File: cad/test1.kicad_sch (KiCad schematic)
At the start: 2 parts

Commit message: docs added
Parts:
- added BT?: Battery, symbol Device:Battery
- added M? (x2): Motor_DC, symbol Motor:Motor_DC
- added U?: MemsicIMU380, symbol teetest:MemsicIMU380
- gave numbers to parts that had none: 1
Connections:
- net at M.~ (VREG): now also BT?.2 (-)
- new net: M.~ (VREG), M?.1 (+) (x2)
- new net: M.~ (VREG), M?.2 (-) (x2)
- new net: BT?.1 (+), M.~ (VREG)
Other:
- moved on the sheet: M, U?

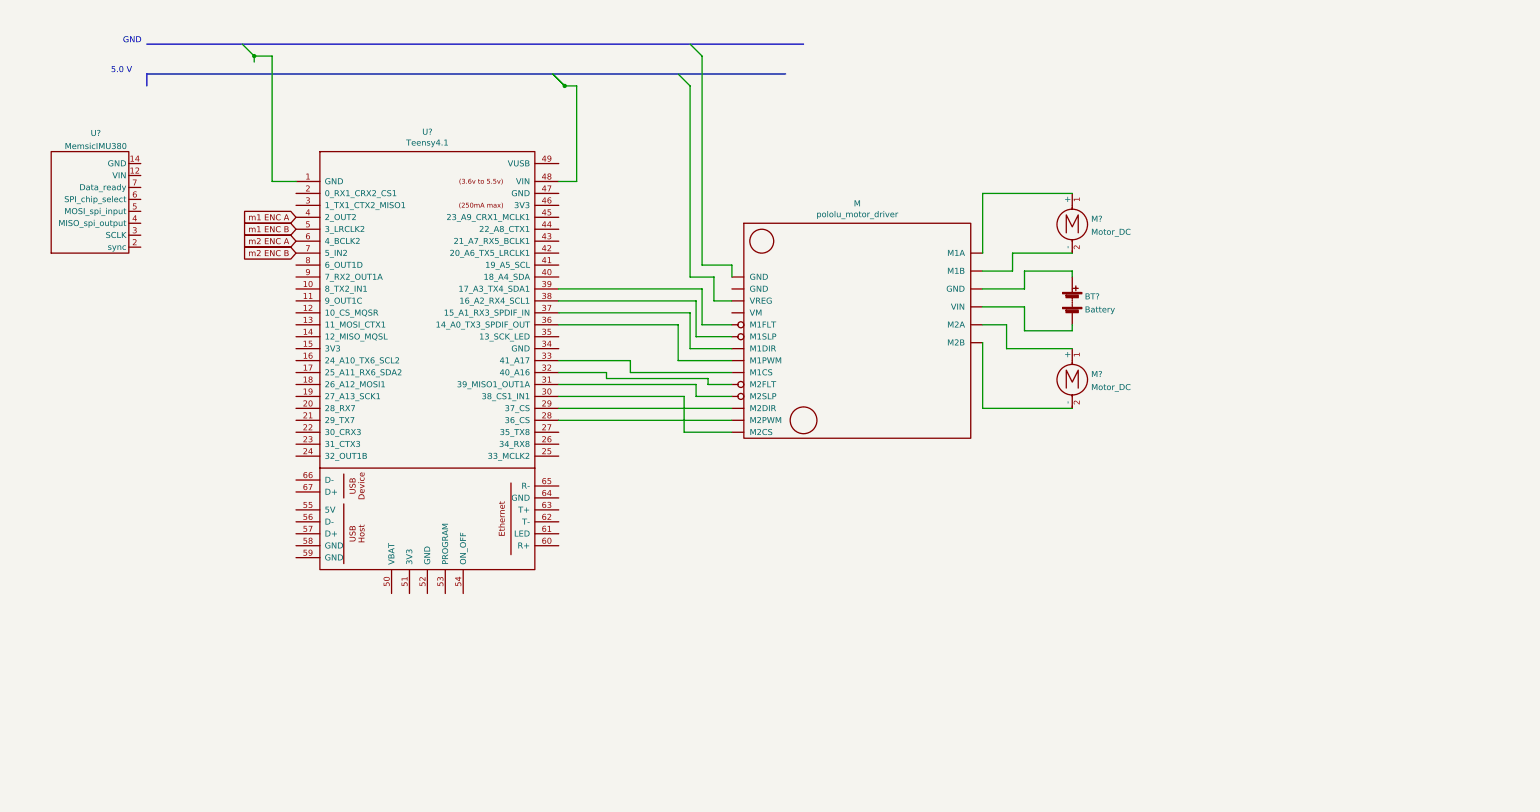
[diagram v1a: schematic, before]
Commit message: audio lib added
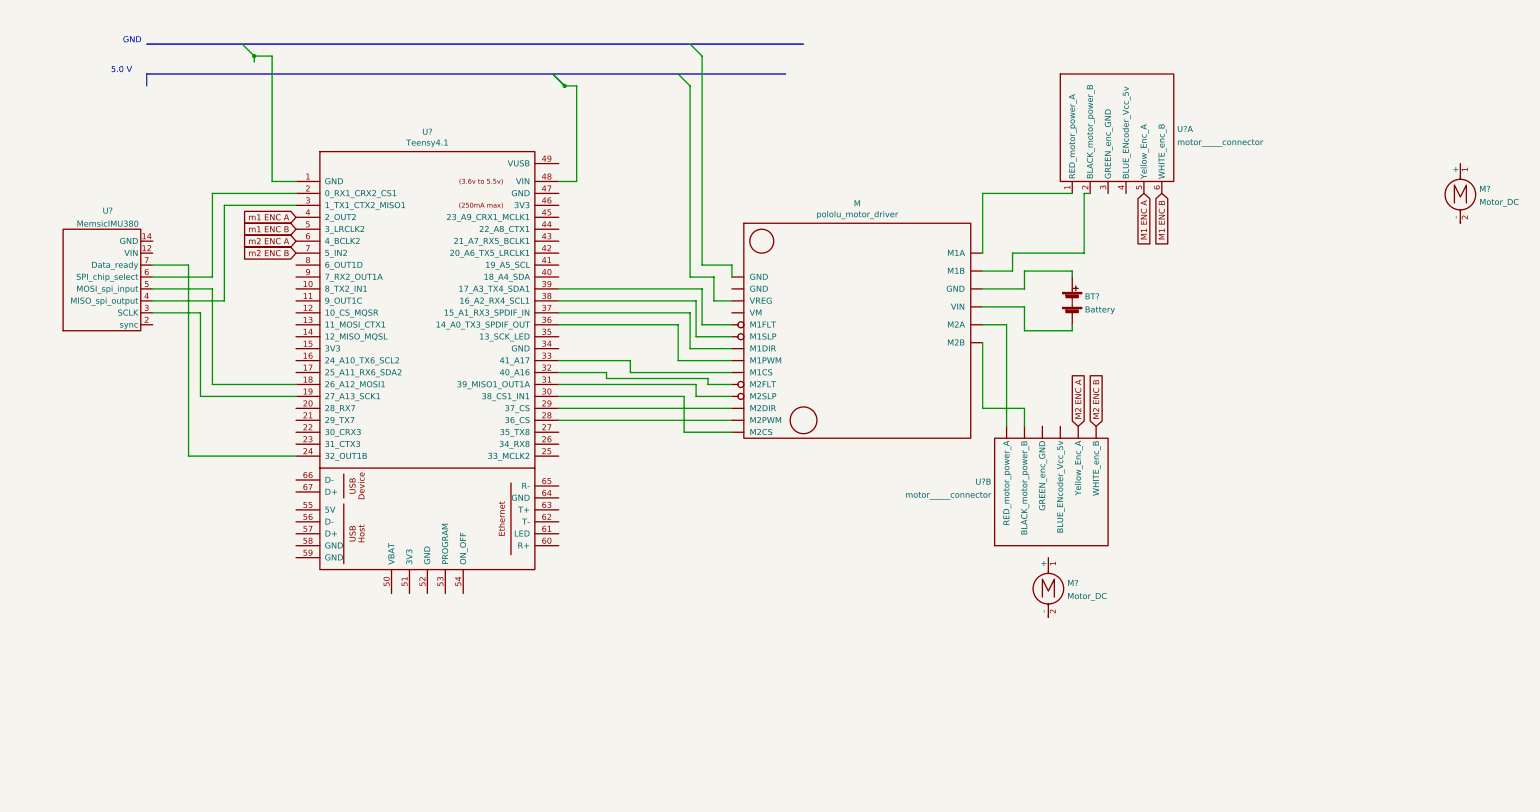
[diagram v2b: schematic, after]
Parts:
- added U? (x2): motor_____connector, symbol teetest:motor_____connector
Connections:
- net at U?.18 (26_A12_MOSI1): now also U?.5 (MOSI_spi_input)
- net at U?.19 (27_A13_SCK1): now also U?.3 (SCLK)
- net at U?.2 (0_RX1_CRX2_CS1): now also U?.6 (SPI_chip_select)
- net at U?.24 (32_OUT1B): now also U?.7 (Data_ready)
- net at U?.3 (1_TX1_CTX2_MISO1): now also U?.4 (MISO_spi_output)
- net at M.~ (VREG): now also BT?.2 (-)
- net at M?.1 (+): no longer M.~ (VREG) (x2)
- net at M?.2 (-): no longer M.~ (VREG) (x2)
- new net: M.~ (VREG), U?.-UB (Yellow_Enc_A)
- new net: M.~ (VREG), U?.1-UB (RED_motor_power_A)
- new net: M.~ (VREG), U?.1 (RED_motor_power_A)
- new net: M.~ (VREG), U?.2 (BLACK_motor_power_B)
- new net M1 ENC A: U?.5 (Yellow_Enc_A)
- new net M1 ENC B: U?.6 (WHITE_enc_B)
- new net M2 ENC A: U?.-UB (Yellow_Enc_A)
- new net M2 ENC B: U?.6-UB (WHITE_enc_B)
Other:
- moved on the sheet: M?, U?
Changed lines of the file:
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@@
+    (stroke (width 0) (type default) (color 0 0 0 0))
+  )
+  (wire (pts (xy 49.53 74.93) (xy 57.15 74.93))
+    (stroke (width 0) (type default) (color 0 0 0 0))
+  )
+  (wire (pts (xy 49.53 77.47) (xy 62.23 77.47))
+    (stroke (width 0) (type default) (color 0 0 0 0))
+  )
+  (wire (pts (xy 49.53 80.01) (xy 62.23 80.01))
+    (stroke (width 0) (type default) (color 0 0 0 0))
+  )
+  (wire (pts (xy 49.53 82.55) (xy 64.77 82.55))
+    (stroke (width 0) (type default) (color 0 0 0 0))
+  )
+  (wire (pts (xy 49.53 85.09) (xy 59.69 85.09))
+    (stroke (width 0) (type default) (color 0 0 0 0))
+  )
+  (wire (pts (xy 57.15 74.93) (xy 57.15 115.57))
+    (stroke (width 0) (type default) (color 0 0 0 0))
+  )
+  (wire (pts (xy 57.15 115.57) (xy 80.01 115.57))
+    (stroke (width 0) (type default) (color 0 0 0 0))
+  )
+  (wire (pts (xy 59.69 85.09) (xy 59.69 102.87))
+    (stroke (width 0) (type default) (color 0 0 0 0))
+  )
+  (wire (pts (xy 59.69 102.87) (xy 80.01 102.87))
+    (stroke (width 0) (type default) (color 0 0 0 0))
+  )
+  (wire (pts (xy 62.23 59.69) (xy 80.01 59.69))
+    (stroke (width 0) (type default) (color 0 0 0 0))
+  )
+  (wire (pts (xy 62.23 77.47) (xy 62.23 59.69))
+    (stroke (width 0) (type default) (color 0 0 0 0))
+  )
+  (wire (pts (xy 62.23 80.01) (xy 62.23 100.33))
+    (stroke (width 0) (type default) (color 0 0 0 0))
+  )
+  (wire (pts (xy 62.23 100.33) (xy 80.01 100.33))
+    (stroke (width 0) (type default) (color 0 0 0 0))
+  )
+  (wire (pts (xy 64.77 62.23) (xy 80.01 62.23))
+    (stroke (width 0) (type default) (color 0 0 0 0))
+  )
+  (wire (pts (xy 64.77 82.55) (xy 64.77 62.23))
     (stroke (width 0) (type default) (color 0 0 0 0))
   )
@@
     (stroke (width 0) (type default) (color 0 0 0 0))
   )
-  (wire (pts (xy 226.06 105.41) (xy 245.11 105.41))
-    (stroke (width 0) (type default) (color 0 0 0 0))
-  )
-  (wire (pts (xy 231.14 87.63) (xy 231.14 92.71))
-    (stroke (width 0) (type default) (color 0 0 0 0))
-  )
-  (wire (pts (xy 231.14 92.71) (xy 245.11 92.71))
-    (stroke (width 0) (type default) (color 0 0 0 0))
-  )
-  (wire (pts (xy 232.41 72.39) (xy 245.11 72.39))
+  (wire (pts (xy 226.06 105.41) (xy 234.95 105.41))
+    (stroke (width 0) (type default) (color 0 0 0 0))
+  )
+  (wire (pts (xy 231.14 87.63) (xy 231.14 109.22))
+    (stroke (width 0) (type default) (color 0 0 0 0))
+  )
+  (wire (pts (xy 232.41 72.39) (xy 247.65 72.39))
     (stroke (width 0) (type default) (color 0 0 0 0))
   )
@@
     (stroke (width 0) (type default) (color 0 0 0 0))
   )
+  (wire (pts (xy 234.95 105.41) (xy 234.95 109.22))
+    (stroke (width 0) (type default) (color 0 0 0 0))
+  )
   (wire (pts (xy 245.11 76.2) (xy 245.11 77.47))
     (stroke (width 0) (type default) (color 0 0 0 0))
   )
   (wire (pts (xy 245.11 87.63) (xy 245.11 88.9))
+    (stroke (width 0) (type default) (color 0 0 0 0))
+  )
+  (wire (pts (xy 247.65 59.69) (xy 247.65 72.39))
+    (stroke (width 0) (type default) (color 0 0 0 0))
+  )
+  (wire (pts (xy 248.92 59.69) (xy 247.65 59.69))
     (stroke (width 0) (type default) (color 0 0 0 0))
   )
@@
     )
   )
+  (global_label "M2 ENC A" (shape input) (at 246.38 109.22 90) (fields_autoplaced)
+    (effects (font (size 1.27 1.27)) (justify left))
+    (property "Intersheet References" "${INTERSHEET_REFS}" (id 0) (at 246.3006 97.3726 90)
+      (effects (font (size 1.27 1.27)) (justify left) hide)
+    )
+  )
+  (global_label "M2 ENC B" (shape input) (at 250.19 109.22 90) (fields_autoplaced)
+    (effects (font (size 1.27 1.27)) (justify left))
+    (property "Intersheet References" "${INTERSHEET_REFS}" (id 0) (at 250.1106 97.1912 90)
+      (effects (font (size 1.27 1.27)) (justify left) hide)
+    )
+  )
+  (global_label "M1 ENC A" (shape input) (at 260.35 59.69 270) (fields_autoplaced)
+    (effects (font (size 1.27 1.27)) (justify right))
+    (property "Intersheet References" "${INTERSHEET_REFS}" (id 0) (at 260.4294 71.5374 90)
+      (effects (font (size 1.27 1.27)) (justify left) hide)
+    )
+  )
+  (global_label "M1 ENC B" (shape input) (at 264.16 59.69 270) (fields_autoplaced)
+    (effects (font (size 1.27 1.27)) (justify right))
+    (property "Intersheet References" "${INTERSHEET_REFS}" (id 0) (at 264.2394 71.7188 90)
+      (effects (font (size 1.27 1.27)) (justify left) hide)
+    )
+  )
   (symbol (lib_id "Device:Battery") (at 245.11 82.55 0) (unit 1)
     (in_bom yes) (on_board yes) (fields_autoplaced)
@@
     (pin "2")
   )
-  (symbol (lib_id "Motor:Motor_DC") (at 245.11 64.77 0) (unit 1)
+  (symbol (lib_id "Motor:Motor_DC") (at 240.03 142.24 0) (unit 1)
     (in_bom yes) (on_board yes) (fields_autoplaced)
-    (property "Reference" "M?" (id 0) (at 249.1233 65.1315 0)
-      (effects (font (size 1.27 1.27)) (justify left))
-    )
-    (property "Value" "Motor_DC" (id 1) (at 249.1233 67.9066 0)
-      (effects (font (size 1.27 1.27)) (justify left))
-    )
-    (property "Footprint" "" (id 2) (at 245.11 67.056 0)
-      (effects (font (size 1.27 1.27)) hide)
-    )
-    (property "Datasheet" "~" (id 3) (at 245.11 67.056 0)
+    (property "Reference" "M?" (id 0) (at 244.0433 142.6015 0)
+      (effects (font (size 1.27 1.27)) (justify left))
+    )
+    (property "Value" "Motor_DC" (id 1) (at 244.0433 145.3766 0)
+      (effects (font (size 1.27 1.27)) (justify left))
+    )
+    (property "Footprint" "" (id 2) (at 240.03 144.526 0)
+      (effects (font (size 1.27 1.27)) hide)
+    )
+    (property "Datasheet" "~" (id 3) (at 240.03 144.526 0)
       (effects (font (size 1.27 1.27)) hide)
     )
@@
     (pin "2")
   )
-  (symbol (lib_id "Motor:Motor_DC") (at 245.11 97.79 0) (unit 1)
+  (symbol (lib_id "Motor:Motor_DC") (at 327.66 58.42 0) (unit 1)
     (in_bom yes) (on_board yes) (fields_autoplaced)
-    (property "Reference" "M?" (id 0) (at 249.1233 98.1515 0)
-      (effects (font (size 1.27 1.27)) (justify left))
-    )
-    (property "Value" "Motor_DC" (id 1) (at 249.1233 100.9266 0)
-      (effects (font (size 1.27 1.27)) (justify left))
-    )
-    (property "Footprint" "" (id 2) (at 245.11 100.076 0)
-      (effects (font (size 1.27 1.27)) hide)
-    )
-    (property "Datasheet" "~" (id 3) (at 245.11 100.076 0)
+    (property "Reference" "M?" (id 0) (at 331.6733 58.7815 0)
+      (effects (font (size 1.27 1.27)) (justify left))
+    )
+    (property "Value" "Motor_DC" (id 1) (at 331.6733 61.5566 0)
+      (effects (font (size 1.27 1.27)) (justify left))
+    )
+    (property "Footprint" "" (id 2) (at 327.66 60.706 0)
+      (effects (font (size 1.27 1.27)) hide)
+    )
+    (property "Datasheet" "~" (id 3) (at 327.66 60.706 0)
       (effects (font (size 1.27 1.27)) hide)
     )
@@
     (pin "2")
   )
-  (symbol (lib_id "teetest:MemsicIMU380") (at 27.94 64.77 90) (unit 1)
+  (symbol (lib_id "teetest:MemsicIMU380") (at 30.48 81.28 90) (unit 1)
     (in_bom yes) (on_board yes) (fields_autoplaced)
-    (property "Reference" "U?" (id 0) (at 37.4269 46.8842 90))
-    (property "Value" "MemsicIMU380" (id 1) (at 37.4269 49.6593 90))
-    (property "Footprint" "" (id 2) (at 26.67 64.77 0)
-      (effects (font (size 1.27 1.27)) hide)
-    )
-    (property "Datasheet" "" (id 3) (at 26.67 64.77 0)
+    (property "Reference" "U?" (id 0) (at 39.9669 63.3942 90))
+    (property "Value" "MemsicIMU380" (id 1) (at 39.9669 66.1693 90))
+    (property "Footprint" "" (id 2) (at 29.21 81.28 0)
+      (effects (font (size 1.27 1.27)) hide)
+    )
+    (property "Datasheet" "" (id 3) (at 29.21 81.28 0)
       (effects (font (size 1.27 1.27)) hide)
     )
@@
     (pin "6")
     (pin "7")
+  )
+  (symbol (lib_name "motor_____connector_1") (lib_id "teetest:motor_____connector") (at 238.76 137.16 0) (mirror x) (unit 2)
+    (in_bom yes) (on_board yes) (fields_autoplaced)
+    (property "Reference" "U?" (id 0) (at 227.8887 121.0496 0)
+      (effects (font (size 1.27 1.27)) (justify right))
+    )
+    (property "Value" "motor_____connector" (id 1) (at 227.8887 123.8247 0)
+      (effects (font (size 1.27 1.27)) (justify right))
+    )
+    (property "Footprint" "" (id 2) (at 238.76 137.16 0)
+      (effects (font (size 1.27 1.27)) hide)
+    )
+    (property "Datasheet" "" (id 3) (at 238.76 137.16 0)
+      (effects (font (size 1.27 1.27)) hide)
+    )
+    (pin "-UB")
+    (pin "-UB")
+    (pin "1-UB")
+    (pin "3-UB")
+    (pin "4-UB")
+    (pin "6-UB")
+  )
+  (symbol (lib_id "teetest:motor_____connector") (at 252.73 31.75 0) (unit 1)
+    (in_bom yes) (on_board yes) (fields_autoplaced)
+    (property "Reference" "U?" (id 0) (at 267.4113 46.0434 0)
+      (effects (font (size 1.27 1.27)) (justify left))
+    )
+    (property "Value" "motor_____connector" (id 1) (at 267.4113 48.8185 0)
+      (effects (font (size 1.27 1.27)) (justify left))
+    )
+    (property "Footprint" "" (id 2) (at 252.73 31.75 0)
+      (effects (font (size 1.27 1.27)) hide)
+    )
+    (property "Datasheet" "" (id 3) (at 252.73 31.75 0)
+      (effects (font (size 1.27 1.27)) hide)
+    )
+    (pin "1")
+    (pin "2")
+    (pin "3")
+    (pin "4")
+    (pin "5")
+    (pin "6")
   )
   (symbol (lib_id "teetest_kikad:pololu_motor_driver") (at 194.31 104.14 0) (unit 1)
@@
       (reference "U?") (unit 1) (value "Teensy4.1") (footprint "")
     )
+    (path "/7b4e6370-1e7f-4098-8f78-08068a47f27f"
+      (reference "U?") (unit 1) (value "motor_____connector") (footprint "")
+    )
     (path "/a87e3b90-a588-4011-86bd-618e89cde162"
       (reference "U?") (unit 1) (value "MemsicIMU380") (footprint "")
     )
-  )
+    (path "/02844968-56f7-454f-a5d0-b9eee3467ebb"
+      (reference "U?") (unit 2) (value "motor_____connector") (footprint "")
+    )
+  )

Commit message: prototype v0.2
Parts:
- added D?: LED, symbol Device:LED
- added R? (x2): R, symbol Device:R
- added U? (x2): logic_level_shifter, symbol teetest:logic_level_shifter
- added U?: IR_receiver, symbol teetest:IR_receiver
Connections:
- net M1 ENC A: now also U?. (LV); no longer U?.5 (Yellow_Enc_A)
- net M1 ENC B: now also U?. (LV); no longer U?.6 (WHITE_enc_B)
- net M2 ENC A: now also U?. (LV); no longer U?.-UB (Yellow_Enc_A)
- net M2 ENC B: now also U?. (LV); no longer U?.6-UB (WHITE_enc_B)
- net at U?.25 (33_MCLK2): now also U?. (LV)
- net IR_input: now reaches U?.8 (6_OUT1D)
- net at M.~ (VREG): now also BT?.2 (-)
- net at U?.-UB (Yellow_Enc_A): now also U?. (LV); no longer M.~ (VREG)
- new net: M.~ (VREG), U?.-UB (Yellow_Enc_A)
- new net: U?. (LV), U?.6-UB (WHITE_enc_B)
- new net: U?. (LV), U?.5 (Yellow_Enc_A)
- new net: U?. (LV), U?.6 (WHITE_enc_B)
- new net: R?.1, R?.2
- new net: D?.2 (A), U?. (LV)
- new net 3.3V: U?. (LV), U?. (LV)
- new net 5V: U?. (LV), U?. (LV)
- new net GND: R?.1
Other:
- moved on the sheet: M?
